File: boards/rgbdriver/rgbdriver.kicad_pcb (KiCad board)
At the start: 2 copper layers, 7 parts, among them U1 rgb.breakout

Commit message: first attempt at copper fill
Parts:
- moved U1 1.55 mm to (150.1, 124.2)
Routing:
- added copper zone on F.Cu, net +24V
- added copper zone on B.Cu, net GNDPWR
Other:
- net class led added: clearance 0.2, trace_width 1, via_dia 0.6, via_drill 0.4
- net class power added: clearance 0.2, trace_width 0.25, via_dia 0.6, via_drill 0.4
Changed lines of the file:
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@@
   (general
     (links 24)
-    (no_connects 24)
-    (area 0 0 0 0)
+    (no_connects 18)
+    (area 141.478 28.448 177.46 126.746001)
     (thickness 1.6)
     (drawings 0)
@@
     (pad_to_mask_clearance 0.2)
     (aux_axis_origin 0 0)
-    (visible_elements FFFFEF7F)
+    (visible_elements FFFFFF7F)
     (pcbplotparams
       (layerselection 0x00030_80000001)
@@
     (uvia_dia 0.3)
     (uvia_drill 0.1)
-    (add_net +24V)
+    (add_net GND)
+    (add_net "Net-(350ma1-Pad5)")
+    (add_net "Net-(350ma2-Pad5)")
+    (add_net "Net-(350ma3-Pad5)")
+    (add_net VCC)
+  )
+  (net_class led ""
+    (clearance 0.2)
+    (trace_width 1)
+    (via_dia 0.6)
+    (via_drill 0.4)
+    (uvia_dia 0.3)
+    (uvia_drill 0.1)
     (add_net /b+)
     (add_net /b-)
@@
     (add_net /r+)
     (add_net /r-)
-    (add_net GND)
+  )
+  (net_class power ""
+    (clearance 0.2)
+    (trace_width 0.25)
+    (via_dia 0.6)
+    (via_drill 0.4)
+    (uvia_dia 0.3)
+    (uvia_drill 0.1)
+    (add_net +24V)
     (add_net GNDPWR)
-    (add_net "Net-(350ma1-Pad5)")
-    (add_net "Net-(350ma2-Pad5)")
-    (add_net "Net-(350ma3-Pad5)")
-    (add_net VCC)
   )
   (module "lighting:350ma constant current xl4001" (layer F.Cu)
@@
   )
   (module lighting:rgb.breakout (layer F.Cu)
-    (at 149.86 125.73)
+    (at 150.114 124.206)
     (fp_text reference U1 (at 15.24 -5.08) (layer F.SilkS)
       (effects (font (size 1 1) (thickness 0.15)))
@@
       (net 10 /b+))
   )
+  (zone (net 4) (net_name GNDPWR) (layer B.Cu) (hatch edge 0.508)
+    (connect_pads (clearance 0.508))
+    (min_thickness 0.254)
+    (fill yes (arc_segments 16) (thermal_gap 0.508) (thermal_bridge_width 0.508))
+    (polygon
+      (pts
+        (xy 141.732 126.746) (xy 148.844 126.746) (xy 148.336 28.448) (xy 141.478 28.448)
+      )
+    )
+  )
+  (zone (net 3) (net_name +24V) (layer F.Cu) (hatch edge 0.508)
+    (connect_pads (clearance 0.508))
+    (min_thickness 0.254)
+    (fill yes (arc_segments 16) (thermal_gap 0.508) (thermal_bridge_width 0.508))
+    (polygon
+      (pts
+        (xy 141.732 126.746) (xy 148.844 126.746) (xy 148.336 28.448) (xy 141.478 28.448)
+      )
+    )
+  )
 )

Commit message: intigial magicstick design
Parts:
- moved 350ma1 58.4 mm to (175.3, 44.5)
- moved R1 58.4 mm to (162.6, 52.1)
- moved 350ma3 29.2 mm to (175.3, 102.9)
- moved R2 29.2 mm to (160.0, 81.3)
- moved 350ma2 29.2 mm to (175.3, 73.7)
- moved R3 29.2 mm to (160.0, 110.5)
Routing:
- net /r-: track 0.00 -> 104.2 mm
- net /g-: track 0.00 -> 82.5 mm
- net /r+: track 0.00 -> 82.4 mm
- net /g+: track 0.00 -> 52.1 mm
- net /b-: track 0.00 -> 37.1 mm
- net /b+: track 0.00 -> 21.8 mm
- removed copper zone on F.Cu, net +24V
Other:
- net class power: trace_width 0.25 -> 1
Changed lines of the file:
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@@
   (general
     (links 24)
-    (no_connects 18)
+    (no_connects 15)
     (area 141.478 28.448 177.46 126.746001)
     (thickness 1.6)
     (drawings 0)
-    (tracks 0)
+    (tracks 25)
     (zones 0)
     (modules 7)
@@
   (net_class power ""
     (clearance 0.2)
-    (trace_width 0.25)
+    (trace_width 1)
     (via_dia 0.6)
     (via_drill 0.4)
@@
   )
   (module "lighting:350ma constant current xl4001" (layer F.Cu)
-    (at 175.26 102.87 90)
+    (at 175.26 44.45 90)
     (fp_text reference 350ma1 (at 5.08 -12.7 90) (layer F.SilkS)
       (effects (font (size 1 1) (thickness 0.15)))
@@
   )
   (module "lighting:350ma constant current xl4001" (layer F.Cu)
-    (at 175.26 44.45 90)
+    (at 175.26 73.66 90)
     (fp_text reference 350ma2 (at 5.08 -12.7 90) (layer F.SilkS)
       (effects (font (size 1 1) (thickness 0.15)))
@@
   )
   (module "lighting:350ma constant current xl4001" (layer F.Cu)
-    (at 175.26 73.66 90)
+    (at 175.26 102.87 90)
     (fp_text reference 350ma3 (at 5.08 -12.7 90) (layer F.SilkS)
       (effects (font (size 1 1) (thickness 0.15)))
@@
   )
   (module Resistors_ThroughHole:Resistor_Horizontal_RM10mm (layer F.Cu)
-    (at 162.56 110.49 180)
+    (at 162.56 52.07 180)
     (descr "Resistor, Axial,  RM 10mm, 1/3W")
     (tags "Resistor Axial RM 10mm 1/3W")
@@
   )
   (module Resistors_ThroughHole:Resistor_Horizontal_RM10mm (layer F.Cu)
-    (at 160.02 52.07 180)
+    (at 160.02 81.28 180)
     (descr "Resistor, Axial,  RM 10mm, 1/3W")
     (tags "Resistor Axial RM 10mm 1/3W")
@@
   )
   (module Resistors_ThroughHole:Resistor_Horizontal_RM10mm (layer F.Cu)
-    (at 160.02 81.28 180)
+    (at 160.02 110.49 180)
     (descr "Resistor, Axial,  RM 10mm, 1/3W")
     (tags "Resistor Axial RM 10mm 1/3W")
@@
       (net 10 /b+))
   )
+  (segment (start 175.26 44.45) (end 163.068 56.642) (width 1) (layer F.Cu) (net 1))
+  (segment (start 163.068 56.642) (end 163.068 121.412) (width 1) (layer F.Cu) (net 1))
+  (segment (start 163.068 121.412) (end 162.814 121.666) (width 1) (layer F.Cu) (net 1))
+  (segment (start 175.26 31.75) (end 175.26 34.29) (width 1) (layer B.Cu) (net 2))
+  (segment (start 160.881122 126.876098) (end 162.814 124.46) (width 1) (layer B.Cu) (net 2))
+  (segment (start 160.90137 119.841789) (end 160.881122 126.876098) (width 1) (layer B.Cu) (net 2))
+  (segment (start 164.338 115.57) (end 160.90137 119.841789) (width 1) (layer B.Cu) (net 2))
+  (segment (start 164.338 45.212) (end 164.338 115.57) (width 1) (layer B.Cu) (net 2))
+  (segment (start 175.26 34.29) (end 164.338 45.212) (width 1) (layer B.Cu) (net 2))
+  (segment (start 162.814 124.46) (end 162.814 124.206) (width 1) (layer B.Cu) (net 2))
+  (segment (start 175.26 73.66) (end 175.26 76.2) (width 1) (layer F.Cu) (net 7))
+  (segment (start 165.354 86.106) (end 165.354 121.666) (width 1) (layer F.Cu) (net 7))
+  (segment (start 175.26 76.2) (end 165.354 86.106) (width 1) (layer F.Cu) (net 7))
+  (segment (start 177.814156 125.730395) (end 174.498 127.508) (width 1) (layer B.Cu) (net 8))
+  (segment (start 175.26 60.96) (end 178.054 60.96) (width 1) (layer B.Cu) (net 8))
+  (segment (start 168.656 127.508) (end 165.354 124.206) (width 1) (layer B.Cu) (net 8))
+  (segment (start 174.498 127.508) (end 168.656 127.508) (width 1) (layer B.Cu) (net 8))
+  (segment (start 179.578 62.484) (end 177.814156 125.730395) (width 1) (layer B.Cu) (net 8))
+  (segment (start 178.054 60.96) (end 179.578 62.484) (width 1) (layer B.Cu) (net 8))
+  (segment (start 167.894 121.666) (end 167.894 110.236) (width 1) (layer F.Cu) (net 10))
+  (segment (start 167.894 110.236) (end 175.26 102.87) (width 1) (layer F.Cu) (net 10))
+  (segment (start 175.26 90.17) (end 175.26 91.948) (width 1) (layer B.Cu) (net 11))
+  (segment (start 175.26 91.948) (end 171.196 96.012) (width 1) (layer B.Cu) (net 11))
+  (segment (start 171.196 96.012) (end 171.196 120.904) (width 1) (layer B.Cu) (net 11))
+  (segment (start 171.196 120.904) (end 167.894 124.206) (width 1) (layer B.Cu) (net 11))
   (zone (net 4) (net_name GNDPWR) (layer B.Cu) (hatch edge 0.508)
     (connect_pads (clearance 0.508))
     (min_thickness 0.254)
-    (fill yes (arc_segments 16) (thermal_gap 0.508) (thermal_bridge_width 0.508))
-    (polygon
-      (pts
-        (xy 141.732 126.746) (xy 148.844 126.746) (xy 148.336 28.448) (xy 141.478 28.448)
-      )
-    )
-  )
-  (zone (net 3) (net_name +24V) (layer F.Cu) (hatch edge 0.508)
-    (connect_pads (clearance 0.508))
-    (min_thickness 0.254)

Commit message: added filled zone
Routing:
- net /r-: track 104.2 -> 100.2 mm
- added copper zone on F.Cu, net +24V
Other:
- board outline added: 40.6 x 101.6 mm
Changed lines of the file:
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@@
   (general
     (links 24)
-    (no_connects 15)
-    (area 141.478 28.448 177.46 126.746001)
+    (no_connects 12)
+    (area 139.624999 27.864999 180.415001 129.615001)
     (thickness 1.6)
-    (drawings 0)
+    (drawings 4)
     (tracks 25)
     (zones 0)
@@
       (net 10 /b+))
   )
+  (gr_line (start 180.34 27.94) (end 139.7 27.94) (angle 90) (layer Edge.Cuts) (width 0.15))
+  (gr_line (start 180.34 129.54) (end 180.34 27.94) (angle 90) (layer Edge.Cuts) (width 0.15))
+  (gr_line (start 139.7 129.54) (end 180.34 129.54) (angle 90) (layer Edge.Cuts) (width 0.15))
+  (gr_line (start 139.7 27.94) (end 139.7 129.54) (angle 90) (layer Edge.Cuts) (width 0.15))
   (segment (start 175.26 44.45) (end 163.068 56.642) (width 1) (layer F.Cu) (net 1))
   (segment (start 163.068 56.642) (end 163.068 121.412) (width 1) (layer F.Cu) (net 1))
   (segment (start 163.068 121.412) (end 162.814 121.666) (width 1) (layer F.Cu) (net 1))
   (segment (start 175.26 31.75) (end 175.26 34.29) (width 1) (layer B.Cu) (net 2))
-  (segment (start 160.881122 126.876098) (end 162.814 124.46) (width 1) (layer B.Cu) (net 2))
-  (segment (start 160.90137 119.841789) (end 160.881122 126.876098) (width 1) (layer B.Cu) (net 2))
+  (segment (start 161.29 124.46) (end 162.814 124.46) (width 1) (layer B.Cu) (net 2))
+  (segment (start 160.90137 119.841789) (end 161.29 124.46) (width 1) (layer B.Cu) (net 2))
   (segment (start 164.338 115.57) (end 160.90137 119.841789) (width 1) (layer B.Cu) (net 2))
   (segment (start 164.338 45.212) (end 164.338 115.57) (width 1) (layer B.Cu) (net 2))
@@
     (connect_pads (clearance 0.508))
     (min_thickness 0.254)
+    (fill yes (arc_segments 16) (thermal_gap 0.508) (thermal_bridge_width 0.508))
+    (polygon
+      (pts
+        (xy 141.732 126.746) (xy 148.844 126.746) (xy 148.336 28.448) (xy 141.478 28.448)
+      )
+    )
+  )
+  (zone (net 3) (net_name +24V) (layer F.Cu) (hatch edge 0.508)
+    (connect_pads (clearance 0.508))
+    (min_thickness 0.254)

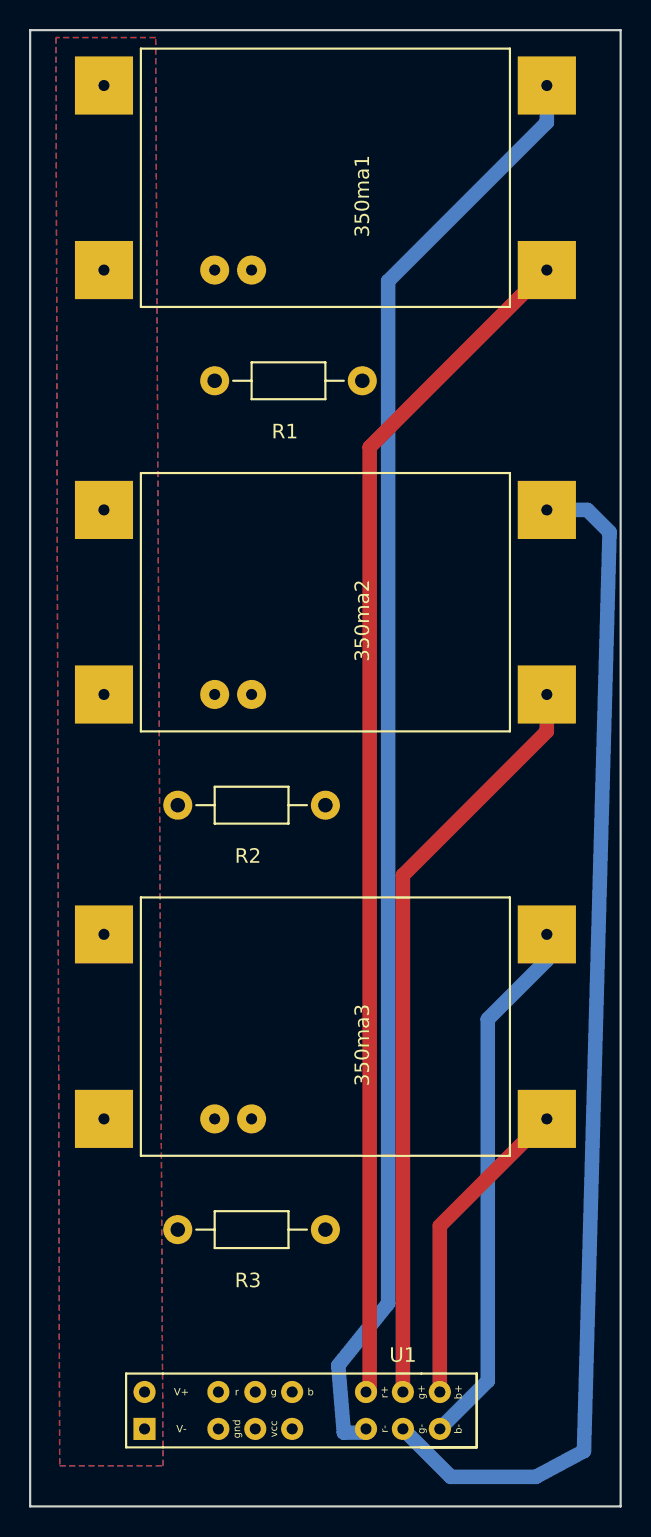
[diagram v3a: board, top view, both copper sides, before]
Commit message: minor rgb driver change
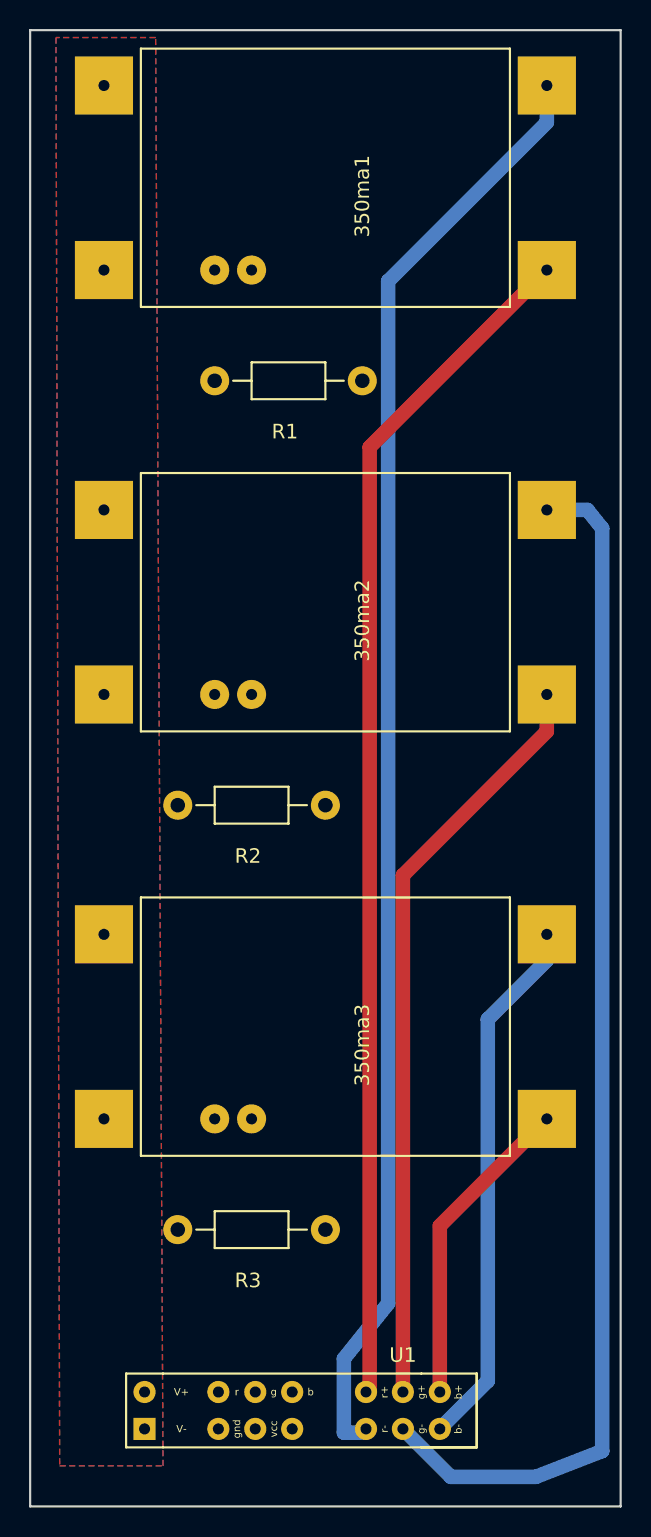
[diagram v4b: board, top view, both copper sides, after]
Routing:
- net /g-: track 82.5 -> 83.3 mm
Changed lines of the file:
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@@
   (segment (start 175.26 31.75) (end 175.26 34.29) (width 1) (layer B.Cu) (net 2))
   (segment (start 161.29 124.46) (end 162.814 124.46) (width 1) (layer B.Cu) (net 2))
-  (segment (start 160.90137 119.841789) (end 161.29 124.46) (width 1) (layer B.Cu) (net 2))
-  (segment (start 164.338 115.57) (end 160.90137 119.841789) (width 1) (layer B.Cu) (net 2))
+  (segment (start 161.29 119.38) (end 161.29 124.46) (width 1) (layer B.Cu) (net 2))
+  (segment (start 164.338 115.57) (end 161.29 119.38) (width 1) (layer B.Cu) (net 2))
   (segment (start 164.338 45.212) (end 164.338 115.57) (width 1) (layer B.Cu) (net 2))
   (segment (start 175.26 34.29) (end 164.338 45.212) (width 1) (layer B.Cu) (net 2))
@@
   (segment (start 165.354 86.106) (end 165.354 121.666) (width 1) (layer F.Cu) (net 7))
   (segment (start 175.26 76.2) (end 165.354 86.106) (width 1) (layer F.Cu) (net 7))
-  (segment (start 177.814156 125.730395) (end 174.498 127.508) (width 1) (layer B.Cu) (net 8))
+  (segment (start 179.07 125.73) (end 174.498 127.508) (width 1) (layer B.Cu) (net 8))
   (segment (start 175.26 60.96) (end 178.054 60.96) (width 1) (layer B.Cu) (net 8))
   (segment (start 168.656 127.508) (end 165.354 124.206) (width 1) (layer B.Cu) (net 8))
   (segment (start 174.498 127.508) (end 168.656 127.508) (width 1) (layer B.Cu) (net 8))
-  (segment (start 179.578 62.484) (end 177.814156 125.730395) (width 1) (layer B.Cu) (net 8))
-  (segment (start 178.054 60.96) (end 179.578 62.484) (width 1) (layer B.Cu) (net 8))
+  (segment (start 179.07 62.23) (end 179.07 125.73) (width 1) (layer B.Cu) (net 8))
+  (segment (start 178.054 60.96) (end 179.07 62.23) (width 1) (layer B.Cu) (net 8))
   (segment (start 167.894 121.666) (end 167.894 110.236) (width 1) (layer F.Cu) (net 10))
   (segment (start 167.894 110.236) (end 175.26 102.87) (width 1) (layer F.Cu) (net 10))

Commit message: autorouter + rj45
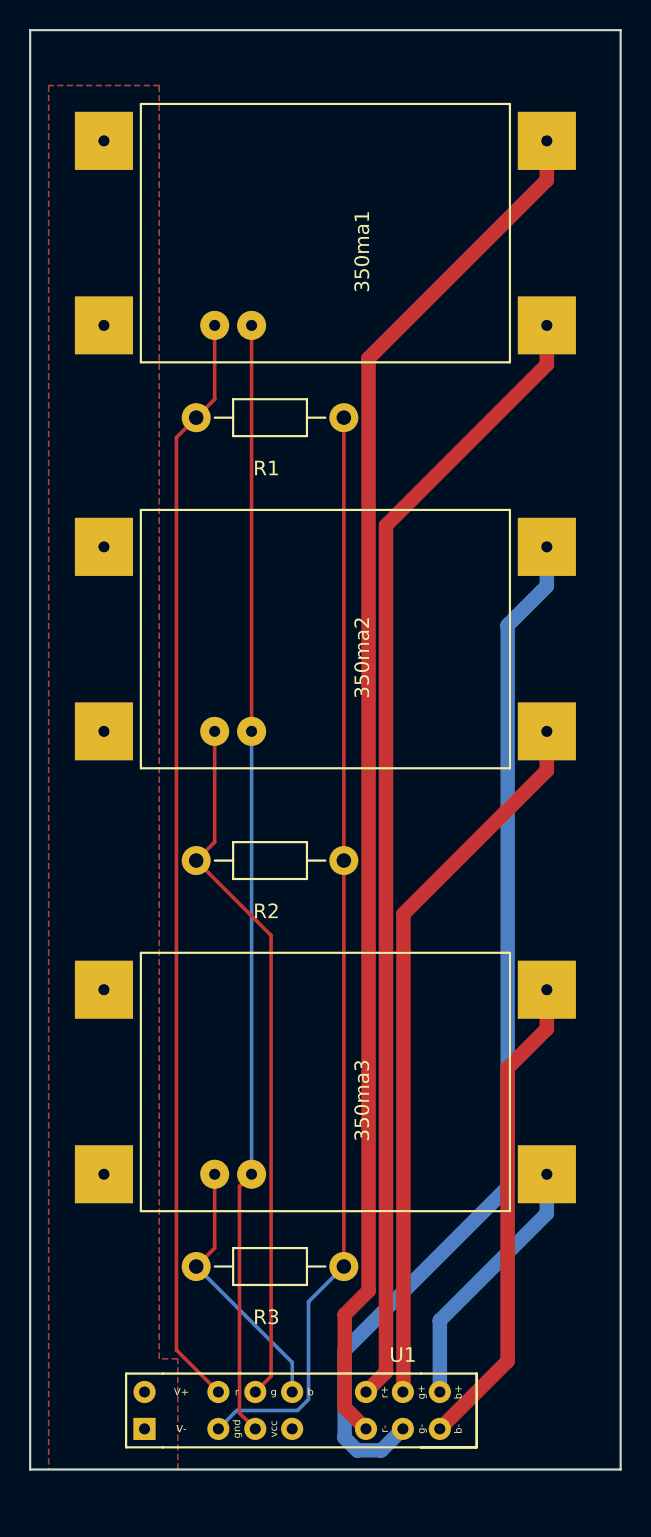
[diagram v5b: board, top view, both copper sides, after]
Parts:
- moved R2 4.02 mm to (161.3, 85.1)
- moved 350ma3 3.81 mm to (175.3, 106.7)
- moved 350ma1 3.81 mm to (175.3, 48.3)
- moved R1 2.84 mm to (161.3, 54.6)
- moved R3 2.84 mm to (161.3, 113.0)
- moved 350ma2 2.54 mm to (175.3, 76.2)
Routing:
- net GND: track 0.00 -> 76.7 mm
- net Net-(350ma1-Pad5): track 0.00 -> 75.7 mm
- net VCC: track 0.00 -> 75.6 mm
- net Net-(350ma2-Pad5): track 0.00 -> 48.6 mm
- net Net-(350ma3-Pad5): track 0.00 -> 18.2 mm
- net /g-: track 83.3 -> 72.1 mm
- net /r-: track 100.1 -> 95.0 mm
- net /r+: track 82.4 -> 78.6 mm
- net /b+: track 21.8 -> 18.0 mm
- net /b-: track 37.1 -> 33.3 mm
- net /g+: track 52.1 -> 49.6 mm
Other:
- board size 40.6 x 101.6 mm -> 40.6 x 99.1 mm

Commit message: initial mother board
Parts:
- 350ma1: moved to B.Cu
- moved R1 52.1 mm to (149.9, 105.4), turned to 270 degrees
- moved 350ma1 38.4 mm to (153.7, 80.0), turned to 0 degrees
- moved R3 29.7 mm to (171.4, 85.1), turned to 270 degrees
- moved R2 20.5 mm to (171.4, 102.9), turned to 270 degrees
- moved 350ma2 20.4 mm to (176.5, 96.5)
- moved 350ma3 8.98 mm to (176.5, 115.6)
- moved U1 2.30 mm to (152.4, 124.5)
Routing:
- net /r-: track 95.0 -> 0.00 mm
- net /r+: track 78.6 -> 0.00 mm
- net GND: track 76.7 -> 0.00 mm
- net Net-(350ma1-Pad5): track 75.7 -> 0.00 mm
- net VCC: track 75.6 -> 0.00 mm
- net /g-: track 72.1 -> 0.00 mm
- net /g+: track 49.6 -> 0.00 mm
- net Net-(350ma2-Pad5): track 48.6 -> 0.00 mm
- net /b-: track 33.3 -> 0.00 mm
- net Net-(350ma3-Pad5): track 18.2 -> 0.00 mm
- net /b+: track 18.0 -> 0.00 mm
- removed copper zone on F.Cu, net +24V
- removed copper zone on B.Cu, net GNDPWR
